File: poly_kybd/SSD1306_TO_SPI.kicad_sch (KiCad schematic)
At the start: 11 parts, among them J29 FH34SRJ-14S-0.5SH

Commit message: Added latest gerber files, latest STLs and updated readme
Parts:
- C2_29: JLC (none) -> C23630; LCSC (none) -> C23630
- renumbered C4_29 to C4_13

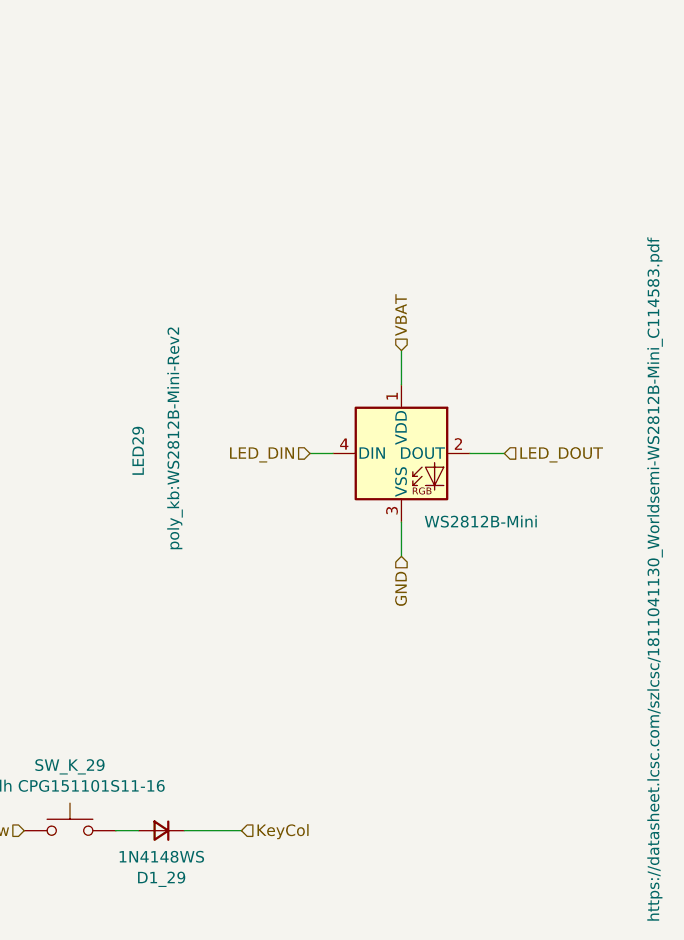
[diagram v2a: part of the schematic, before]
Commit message: Replaced RGB LEDs with XL-3030RGBC-WS2812B and exported new gerbers (v3.1)
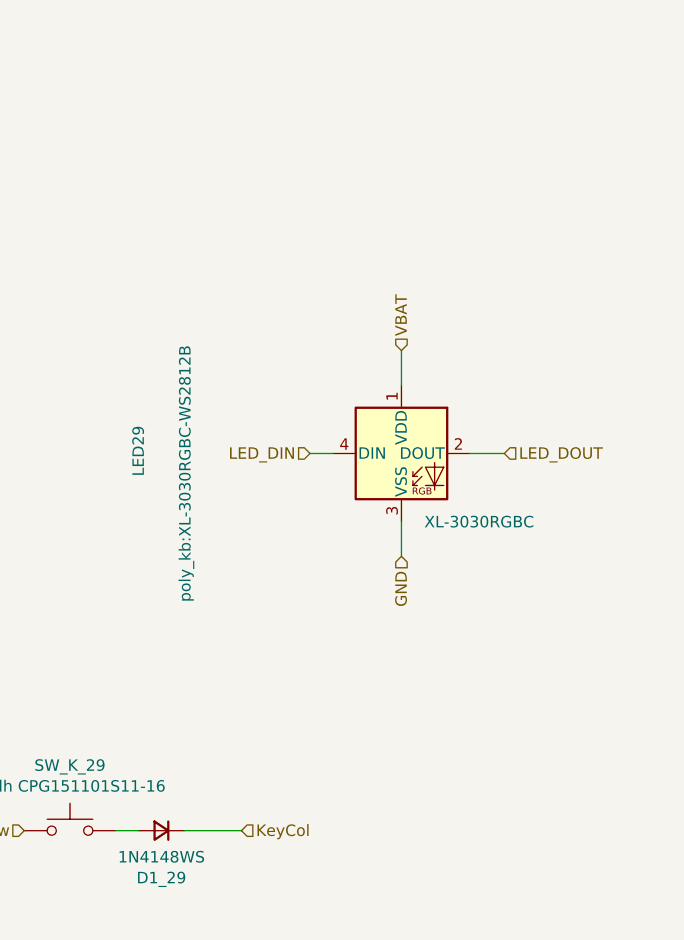
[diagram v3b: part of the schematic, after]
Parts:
- LED29: value WS2812B-Mini -> XL-3030RGBC; footprint poly_kb:WS2812B-Mini-Rev2 -> poly_kb:XL-3030RGBC-WS2812B; MPN C527089 -> C5349958
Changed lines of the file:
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@@
   (title_block
     (title "Display Adapter, LED & Switch")
-    (date "2022-11-16")
-    (rev "2.2")
+    (date "2024-01-08")
+    (rev "3.1")
     (company "thpoll")
   )
@@
       (effects (font (size 1.27 1.27)) (justify left))
     )
-    (property "Value" "WS2812B-Mini" (at 168.91 55.88 0)
+    (property "Value" "XL-3030RGBC" (at 168.91 55.88 0)
       (effects (font (size 1.27 1.27)) (justify left))
     )
-    (property "Footprint" "poly_kb:WS2812B-Mini-Rev2" (at 140.335 59.055 90)
+    (property "Footprint" "poly_kb:XL-3030RGBC-WS2812B" (at 141.605 64.77 90)
       (effects (font (size 1.27 1.27)) (justify left top))
     )
-    (property "Datasheet" "https://datasheet.lcsc.com/szlcsc/1811041130_Worldsemi-WS2812B-Mini_C114583.pdf" (at 193.675 100.33 90)
-      (effects (font (size 1.27 1.27)) (justify left top))
+    (property "Datasheet" "https://datasheet.lcsc.com/lcsc/2301111010_XINGLIGHT-XL-3030RGBC-WS2812B_C5349958.pdf" (at 193.675 100.33 90)
+      (effects (font (size 1.27 1.27)) (justify left top) hide)
     )
     (property "LCSC" "" (at 172.72 41.91 0)
@@
       (effects (font (size 1.27 1.27)) hide)
     )
-    (property "MPN" "C527089" (at 166.37 48.26 0)
-      (effects (font (size 1.27 1.27)) hide)
-    )
+    (property "MPN" "C5349958" (at 166.37 48.26 0)
+      (effects (font (size 1.27 1.27)) hide)
+    )

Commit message: Revision D caps and schematics part cleanup
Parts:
- C1_29: JLC (none) -> C99227; LCSC (none) -> C99227
- C3_29, C5_29, C6_29: JLC (none) -> C52923; LCSC (none) -> C52923
- C4_13: JLC (none) -> C129569; LCSC (none) -> C129569
- D1_29: JLC (none) -> C2128; LCSC (none) -> C2128
- J29: Etc (none) -> Alternative C466533; JLC (none) -> C324724; LCSC (none) -> C324724
- LED29: JLC (none) -> C5349958; LCSC (none) -> C5349958
- R1_29: JLC (none) -> C25744; LCSC (none) -> C25744
- SW_K_29: Etc C5156480 -> (none); JLC (none) -> C5156480; LCSC (none) -> C5156480; MPN (none) -> C5156480
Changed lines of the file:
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@@
       (effects (font (size 1.27 1.27)) hide)
     )
-    (property "LCSC" "" (at 68.58 50.8 90)
-      (effects (font (size 1.27 1.27)))
-    )
-    (property "JLC" "" (at 68.58 46.99 0)
+    (property "LCSC" "C52923" (at 68.58 50.8 90)
+      (effects (font (size 1.27 1.27)))
+    )
+    (property "JLC" "C52923" (at 68.58 46.99 0)
       (effects (font (size 1.27 1.27)) hide)
     )
@@
       (effects (font (size 1.27 1.27)) (justify left top) hide)
     )
-    (property "LCSC" "" (at 172.72 41.91 0)
+    (property "LCSC" "C5349958" (at 172.72 41.91 0)
       (effects (font (size 1.27 1.27)) (justify bottom))
     )
-    (property "JLC" "" (at 166.37 48.26 0)
+    (property "JLC" "C5349958" (at 166.37 48.26 0)
       (effects (font (size 1.27 1.27)) hide)
     )
@@
       (effects (font (size 1.27 1.27)) hide)
     )
+    (property "JLC" "C129569" (at 54.61 69.85 0)
+      (effects (font (size 1.27 1.27)) hide)
+    )
+    (property "LCSC" "C129569" (at 54.61 69.85 0)
+      (effects (font (size 1.27 1.27)) hide)
+    )
     (pin "1")
     (pin "2")
@@
       (effects (font (size 1.27 1.27)) hide)
     )
-    (property "LCSC" "" (at 71.628 77.851 0)
-      (effects (font (size 1.27 1.27)))
-    )
-    (property "JLC" "" (at 67.31 74.93 0)
+    (property "LCSC" "C99227" (at 71.628 77.851 0)
+      (effects (font (size 1.27 1.27)))
+    )
+    (property "JLC" "C99227" (at 67.31 74.93 0)
       (effects (font (size 1.27 1.27)) hide)
     )
@@
       (effects (font (size 1.27 1.27)) hide)
     )
-    (property "LCSC" "" (at 49.53 41.91 90)
-      (effects (font (size 1.27 1.27)))
-    )
-    (property "JLC" "" (at 57.15 41.91 0)
+    (property "LCSC" "C52923" (at 49.53 41.91 90)
+      (effects (font (size 1.27 1.27)))
+    )
+    (property "JLC" "C52923" (at 57.15 41.91 0)
       (effects (font (size 1.27 1.27)) hide)
     )
@@
       (effects (font (size 1.27 1.27)) hide)
     )
-    (property "LCSC" "" (at 31.75 50.8 90)
-      (effects (font (size 1.27 1.27)))
-    )
-    (property "JLC" "" (at 31.75 48.26 0)
+    (property "LCSC" "C52923" (at 31.75 50.8 90)
+      (effects (font (size 1.27 1.27)))
+    )
+    (property "JLC" "C52923" (at 31.75 48.26 0)
       (effects (font (size 1.27 1.27)) hide)
     )
@@
       (effects (font (size 1.27 1.27)) hide)
     )
-    (property "MPN" "" (at 129.54 90.17 0)
-      (effects (font (size 1.27 1.27)) hide)
-    )
-    (property "Etc" "C5156480" (at 129.54 90.17 0)
+    (property "MPN" "C5156480" (at 129.54 90.17 0)
+      (effects (font (size 1.27 1.27)) hide)
+    )
+    (property "Etc" "" (at 129.54 90.17 0)
+      (effects (font (size 1.27 1.27)) hide)
+    )
+    (property "JLC" "C5156480" (at 129.54 90.17 0)
+      (effects (font (size 1.27 1.27)) hide)
+    )
+    (property "LCSC" "C5156480" (at 129.54 90.17 0)
       (effects (font (size 1.27 1.27)) hide)
     )
@@
       (effects (font (size 1.27 1.27)) hide)
     )
-    (property "LCSC" "" (at 139.7 99.06 0)
-      (effects (font (size 1.27 1.27)))
-    )
-    (property "JLC" "" (at 139.7 90.17 0)
+    (property "LCSC" "C2128" (at 139.7 99.06 0)
+      (effects (font (size 1.27 1.27)))
+    )
+    (property "JLC" "C2128" (at 139.7 90.17 0)
       (effects (font (size 1.27 1.27)) hide)
     )
@@
       (effects (font (size 1.27 1.27)) hide)
     )
-    (property "LCSC" "" (at 33.02 57.15 0)
-      (effects (font (size 1.27 1.27)) hide)
-    )
-    (property "JLC" "" (at 33.02 57.15 0)
+    (property "LCSC" "C25744" (at 33.02 57.15 0)
+      (effects (font (size 1.27 1.27)) hide)
+    )
+    (property "JLC" "C25744" (at 33.02 57.15 0)
       (effects (font (size 1.27 1.27)) hide)
     )
@@
       (effects (font (size 1.27 1.27)) hide)
     )
-    (property "LCSC" "" (at 82.55 34.925 0)
+    (property "LCSC" "C324724" (at 82.55 34.925 0)
       (effects (font (size 1.27 1.27)))
     )
@@
       (effects (font (size 1.27 1.27)) hide)
     )
+    (property "Etc" "Alternative C466533" (at 82.55 54.61 0)
+      (effects (font (size 1.27 1.27)) hide)
+    )
+    (property "JLC" "C324724" (at 82.55 54.61 0)
+      (effects (font (size 1.27 1.27)) hide)
+    )

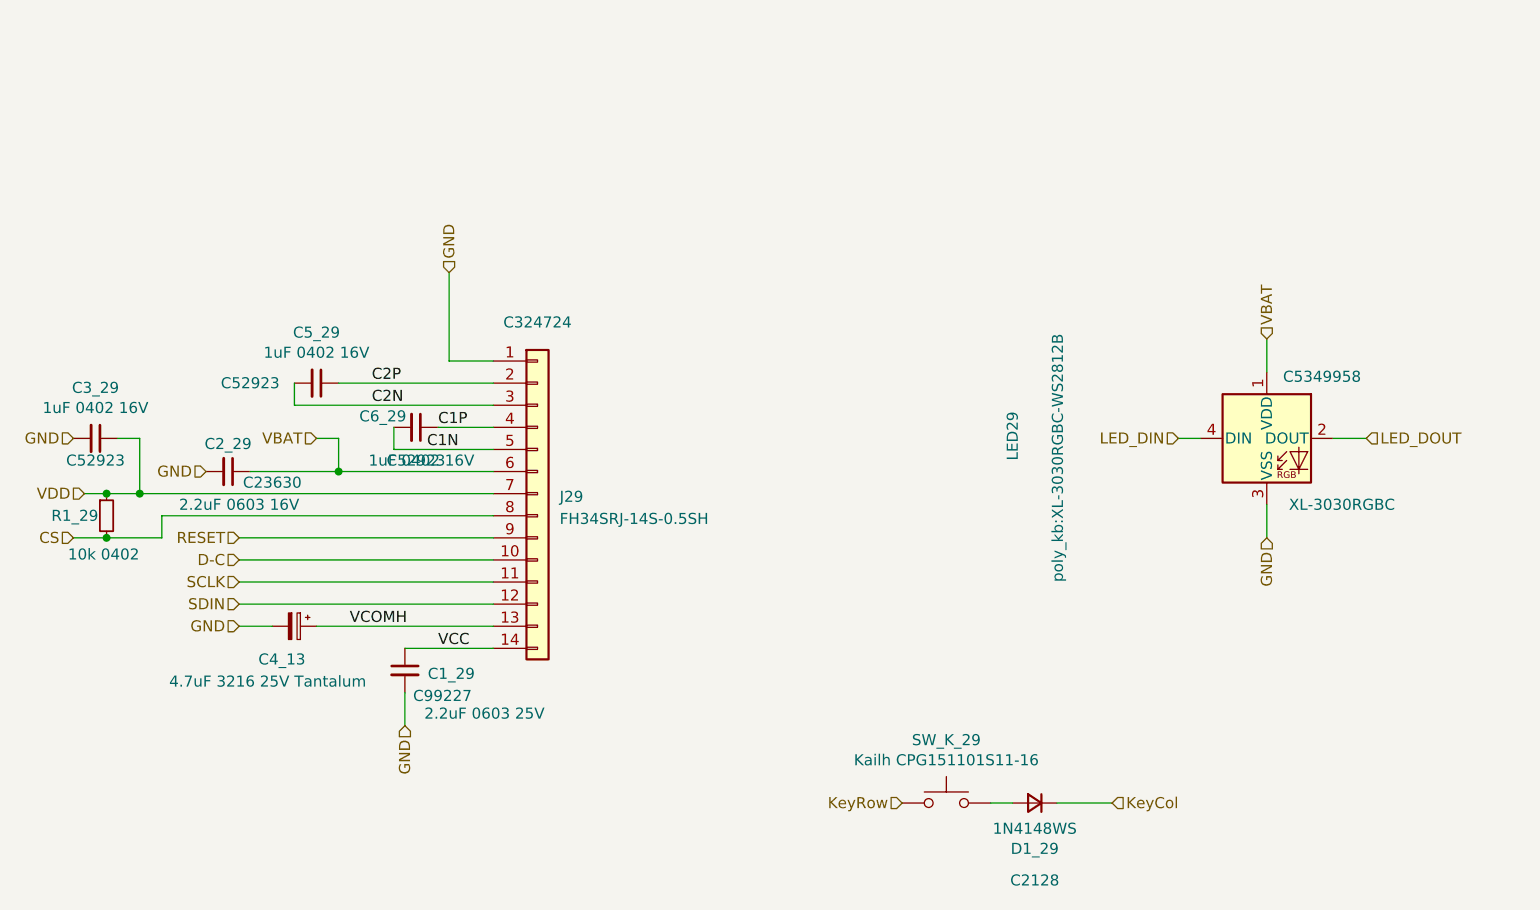
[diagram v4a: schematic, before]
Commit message: Updated left side for RoHS
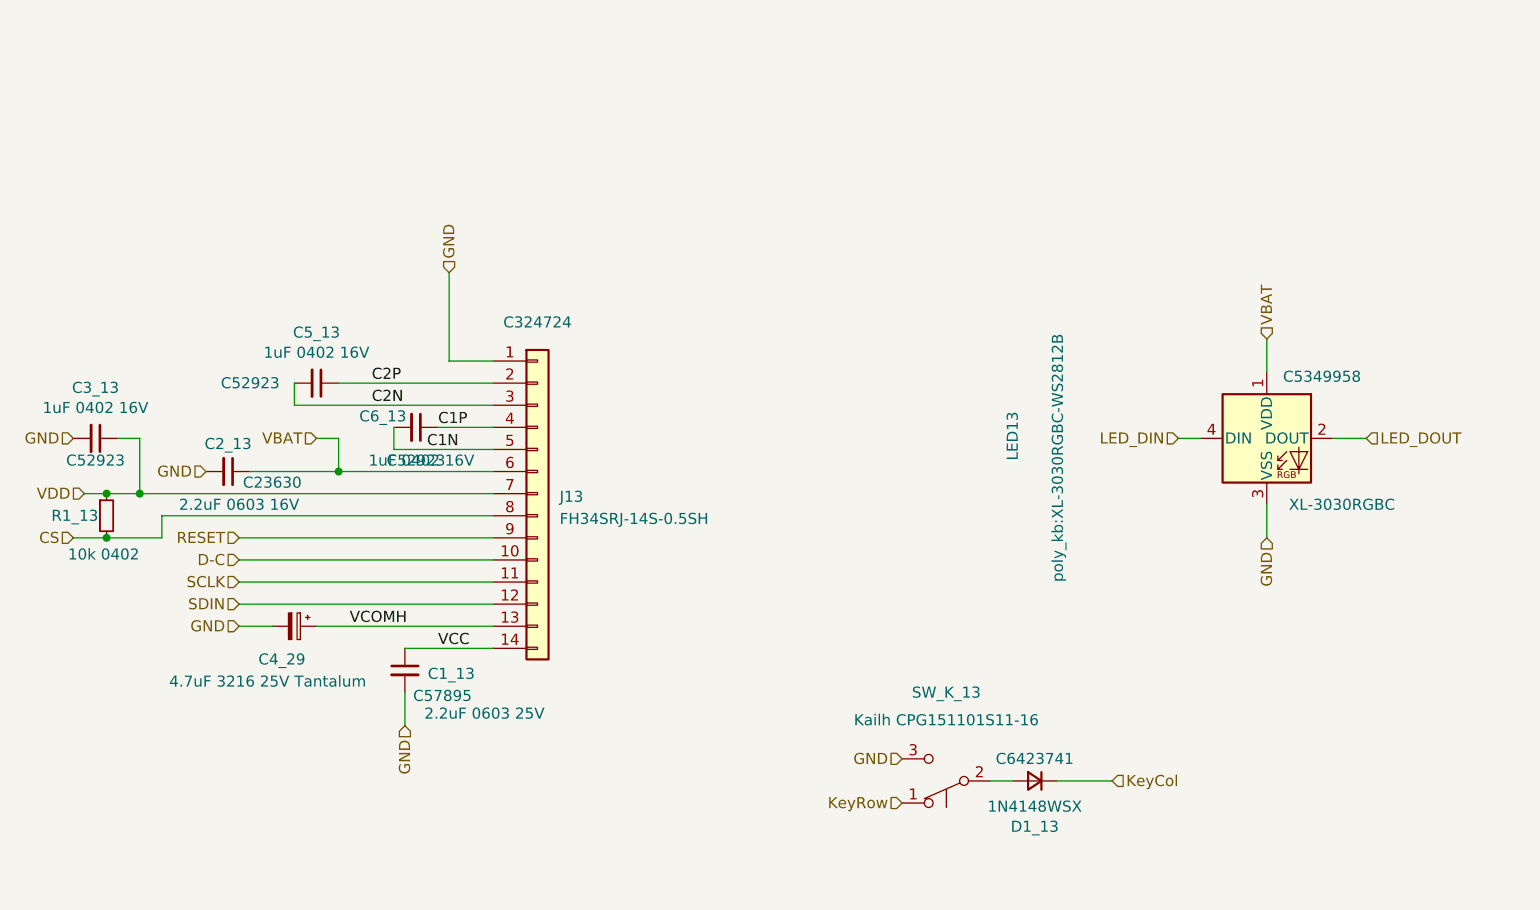
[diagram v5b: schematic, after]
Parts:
- C1_13: renamed from C1_29; JLC C99227 -> C57895; LCSC C99227 -> C57895; MPN C99227 -> C57895; Manufacturer (none) -> Samsung; RoHS (none) -> x
- C2_13: renamed from C2_29; Manufacturer (none) -> Samsung; RoHS (none) -> x
- C3_13: renamed from C3_29; Manufacturer (none) -> Samsung; RoHS (none) -> x
- C4_29: renamed from C4_13; Etc (none) -> Preorder Req; JLC C129569 -> C118249; LCSC C129569 -> C118249; MPN C129569 -> C118249; Manufacturer (none) -> Sunlord; RoHS (none) -> x
- C5_13: renamed from C5_29; Manufacturer (none) -> Samsung; RoHS (none) -> x
- C6_13: renamed from C6_29; Manufacturer (none) -> Samsung; RoHS (none) -> x
- D1_13: renamed from D1_29; value 1N4148WS -> 1N4148WSX; JLC C2128 -> C6423741; LCSC C2128 -> C6423741; MPN C2128 -> C6423741; Manufacturer (none) -> Shenzhen JingYang; RoHS (none) -> x
- J13: renamed from J29; Manufacturer (none) -> JUSHUO; RoHS (none) -> Both x
- LED13: renamed from LED29; Manufacturer (none) -> Xinglight; RoHS (none) -> x
- R1_13: renamed from R1_29; JLC C25744 -> C60490; LCSC C25744 -> C60490; MPN C25744 -> C60490; Manufacturer (none) -> Yageo; RoHS (none) -> x
- SW_K_13: renamed from SW_K_29; symbol Switch:SW_Push -> Switch:SW_Push_SPDT; Etc (none) -> Own Stock; Manufacturer (none) -> Kailh; RoHS (none) -> x
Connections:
- net GND: now also SW_K_13.3 (C)
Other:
- moved on the sheet: D1_13

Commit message: Renamed schematics and pcb files; cleanup; Updated left side to 3.2; Added submodules
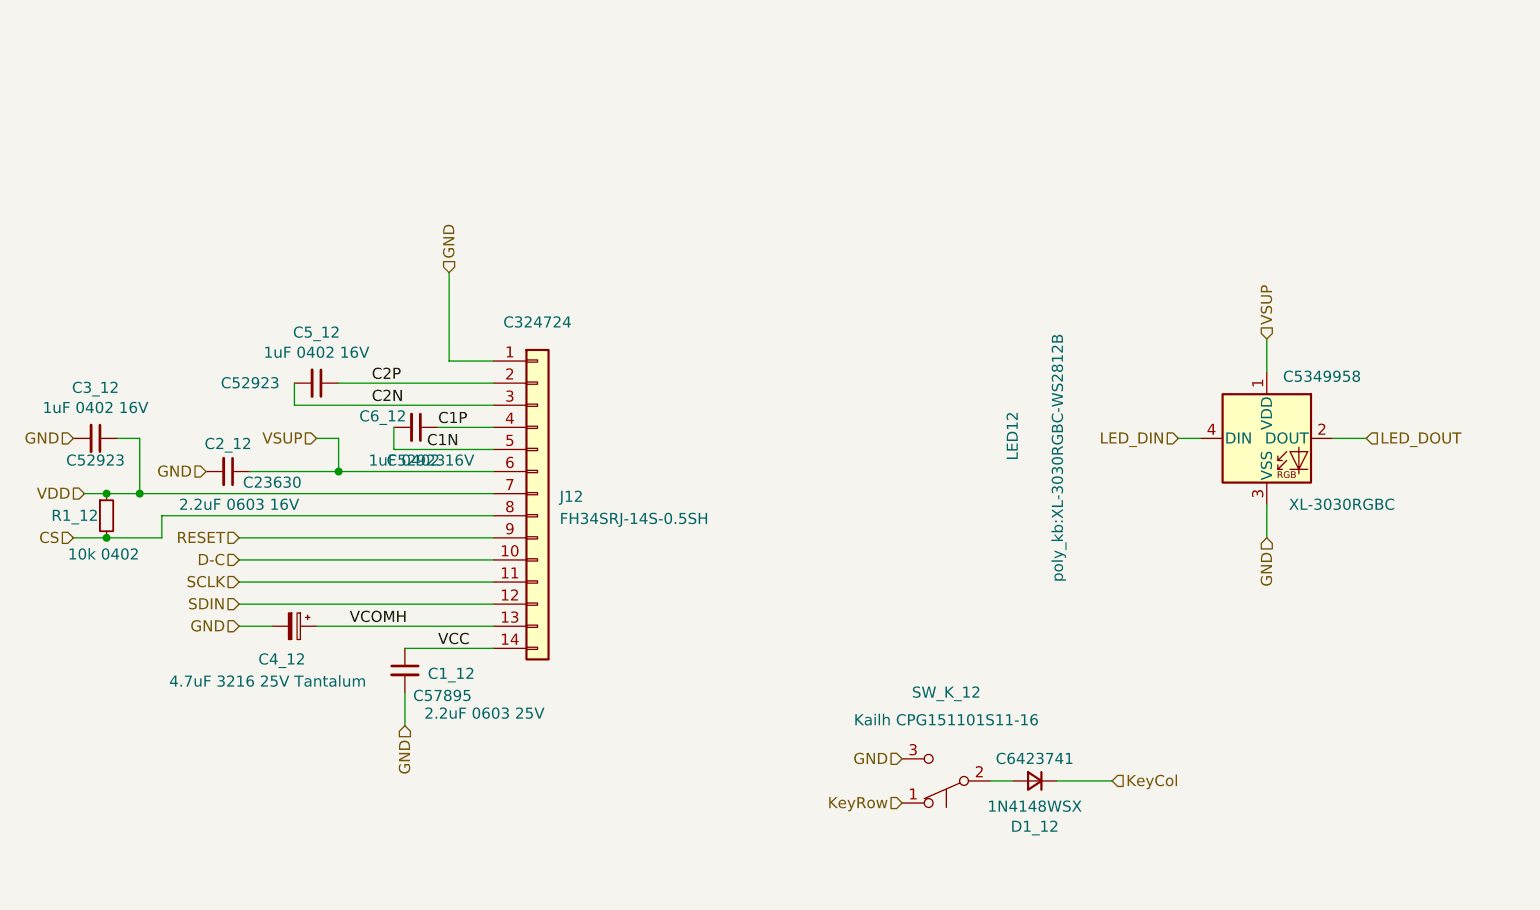
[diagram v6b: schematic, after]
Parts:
- renumbered C1_13 to C1_12, C2_13 to C2_12, C3_13 to C3_12, C4_29 to C4_12, C5_13 to C5_12, C6_13 to C6_12, D1_13 to D1_12, J13 to J12, LED13 to LED12, R1_13 to R1_12, SW_K_13 to SW_K_12
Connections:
- net VBAT renamed VSUP
